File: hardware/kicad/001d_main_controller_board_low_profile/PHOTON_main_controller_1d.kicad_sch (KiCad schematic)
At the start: 61 parts, among them J1 JST_SH, J2 JST_SH, J3 USB_C_Receptacle_USB2.0, SW1 SW_SPST, SW2 SW_SPST, U1 RP2350_60QFN, U2 NCP1117-3.3_SOT223, U3 W25Q128JVPIQ, U4 TPD4E05U06DQAR, U5 THVD1424RGTR, Y1 ABM8-272-T3

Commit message: Main Controller Board (1D) now added. Cheaper design, with RP2354, and BUCK PMIC
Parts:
- removed C22: 100nF, Capacitor_SMD:C_0402_1005Metric, symbol Device:C
- removed H1, H2, H3, H4: MountingHole, MountingHole:MountingHole_2.7mm_M2.5, symbol Mechanical:MountingHole
- removed J2: JST_SH, Connector_JST:JST_SH_SM04B-SRSS-TB_1x04-1MP_P1.00mm_Horizontal, symbol Connector_Generic:Conn_01x04
- removed J4: (no value), Connector_PinHeader_1.27mm:PinHeader_1x04_P1.27mm_Vertical, symbol Connector_Generic:Conn_01x04
- removed JP101: SolderJumper_2_Open, Jumper:SolderJumper-2_P1.3mm_Open_RoundedPad1.0x1.5mm, symbol Jumper:SolderJumper_2_Open
- removed JP2: SolderJumper_2_Bridged, Jumper:SolderJumper-2_P1.3mm_Bridged_RoundedPad1.0x1.5mm, symbol Jumper:SolderJumper_2_Bridged
- removed R13, R14: 22Ω, Resistor_SMD:R_0402_1005Metric, symbol Device:R
- removed R15: DNF, Resistor_SMD:R_0402_1005Metric, symbol Device:R
- removed R17: 100kΩ, Resistor_SMD:R_0402_1005Metric, symbol Device:R
- removed R4: 120 Ω, Resistor_SMD:R_0402_1005Metric, symbol Device:R
- removed SW1, SW2: SW_SPST, footprints:SW-TH_MSK12C02, symbol spst:MSK12C02
- removed U2: NCP1117-3.3_SOT223, Package_TO_SOT_SMD:SOT-223-3_TabPin2, symbol Regulator_Linear:NCP1117-3.3_SOT223
- removed U3: W25Q128JVPIQ, footprints:WSON_128JVPIQ_WIN, symbol Memory_Flash:W25Q128JVS
- removed U5: THVD1424RGTR, footprints:QFN_24RGTR_TEX, symbol 2025-11-21_08-29-10_THVD1424RGTR:THVD1424RGTR
- added C105: 100nF, Capacitor_SMD:C_0402_1005Metric, symbol Device:C
- added C106: 1μF, Capacitor_SMD:C_0402_1005Metric, symbol Device:C
- added CR101: H7VHD3UA, Diode_SMD:D_SOD-323, symbol 2025-08-11_08-49-29:SMF5.0A
- added D10, D11: D_TVS, Diode_SMD:D_SOD-523, symbol Device:D_Schottky
- added H101, H102, H103, H104: MountingHole, MountingHole:MountingHole_2.7mm_M2.5_ISO7380, symbol Mechanical:MountingHole
- added J102: JST_SH RS-485_1, Connector_JST:JST_SH_SM04B-SRSS-TB_1x04-1MP_P1.00mm_Horizontal, symbol Connector_Generic:Conn_01x04
- added J103, J104: JST_SH RS-485_2, Connector_JST:JST_SH_SM04B-SRSS-TB_1x04-1MP_P1.00mm_Horizontal, symbol Connector_Generic:Conn_01x04
- added J4: Micro_SD_Card, Pretty Custom:TF-015_corrected, symbol Connector:Micro_SD_Card
- added JP101: Jumper_2_Open, Jumper:SolderJumper-2_P1.3mm_Open_Pad1.0x1.5mm, symbol Jumper:Jumper_2_Open
- added L2: 1 uH, Inductor_SMD:L_1008_2520Metric, symbol Device:L
- added R103: 100kΩ, Resistor_SMD:R_0402_1005Metric, symbol Device:R
- added R104: 300kΩ, Resistor_SMD:R_0402_1005Metric, symbol Device:R
- added R105: 150kΩ, Resistor_SMD:R_0402_1005Metric, symbol Device:R
- added R236, R237: 2.2kΩ, Resistor_SMD:R_0402_1005Metric, symbol Device:R
- added U102: THVD1424RGTR, Pretty Custom:QFN_24RGTR_TEX, symbol 2025-11-21_08-29-10_THVD1424RGTR:THVD1424RGTR
- added U5: TPS62A0569ADRLR, Pretty Custom:DRL0006A-MFG, symbol TI BUCK:TPS62A0569ADRLR
- C1: value 10uF -> 4.7uF; JLCPCB Part # (none) -> C1779; Part # (none) -> CL21A475KAQNNNE
- C2, C3: footprint footprints:C_0402_1005Metric_small_pads -> RP2350_60QFN_minimal:C_0402_1005Metric_small_pads
- C4: value 10uF -> 22uF; JLCPCB Part # (none) -> C45783
- CR1: value PTVSHC3D7VU -> H7VHD3UA; footprint footprints:SOD-323_L1.8-W1.3-LS2.5-RD -> Diode_SMD:D_SOD-323; symbol PTVSHC3D7VU:PTVSHC3D7VU -> 2025-08-11_08-49-29:SMF5.0A; LCSC Part C110753 -> (none)
- CR5: renamed from CR2; value PTVSHC3D7VU -> H7VHD3UA; footprint footprints:SOD-323_L1.8-W1.3-LS2.5-RD -> Diode_SMD:D_SOD-323; symbol PTVSHC3D7VU:PTVSHC3D7VU -> 2025-08-11_08-49-29:SMF5.0A; LCSC Part C110753 -> (none)
- L1: footprint footprints:L_pol_2016 -> RP2350_60QFN_minimal:L_pol_2016
- R101: value 120 Ω -> 22Ω
- R102: value 10kΩ -> 33Ω
- U1: value RP2350_60QFN -> RP2354_60QFN; footprint footprints:RP2350-QFN-60-1EP_7x7_P0.4mm_EP3.4x3.4mm_ThermalVias -> RP2350_60QFN_minimal:RP2350-QFN-60-1EP_7x7_P0.4mm_EP3.4x3.4mm_ThermalVias; JLCPCB Part # C42411118 -> C41378174
- U4: footprint footprints:DQA0010A -> Pretty Custom:DQA0010A
- renumbered C9 to C103, C10 to C104, J1 to J101, R20 to R233
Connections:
- net +3V3: now also C105.1, C106.1, CR101.1, J102.2 (Pin_2), J103.2 (Pin_2), J104.2 (Pin_2), J4.4 (VDD), L2.2, R104.1, R236.2, R237.2, U102.13 (VIO), U102.14 (VCC), U102.15 (H/F); no longer R102.2
- net GND: now also C105.2, C106.2, CR101.2, D10.2 (A), D11.2 (A), J102.1 (Pin_1), J103.1 (Pin_1), J104.1 (Pin_1), J4.6 (VSS), JP101.1 (A), R103.2, U102.17 (GND), U102.6 (GND), U5.2 (GND)
- net GPIO10: now also J4.5 (CLK)
- net GPIO11: now also J4.3 (CMD)
- net GPIO12: now also J4.7 (DAT0)
- net GPIO13: now also J4.2 (DAT3/CD)
- net GPIO16: now also R101.2
- net GPIO17: now also R102.2
- net GPIO18: now also U102.5 (TERM_TX), U102.7 (TERM_RX)
- net GPIO22: no longer R19.2
- net GPIO23: no longer R233.2
- net GPIO4: now also R19.2
- net RS485_N: now also J102.4 (Pin_4), J103.4 (Pin_4), J104.4 (Pin_4), U102.10 (Z); no longer J101.4 (Pin_4)
- net RS485_P: now also J102.3 (Pin_3), J103.3 (Pin_3), J104.3 (Pin_3), U102.9 (Y); no longer J101.3 (Pin_3), R101.2
- net RUN: no longer R102.1
- net UART_RX: now also U102.1 (R)
- net UART_TX: now also U102.4 (D)
- net ~{USB_BOOT}: now also JP101.2 (B)
- net at C1.1, FB1.2: now also U5.3 (VIN), U5.5 (EN)
- net I2C_0_SDA: now reaches R101.1
- net I2C_0_SDA: now also J101.3 (Pin_3), D10.1 (K), R236.1
- net BANK_0_CS renamed GPIO21
- net BANK_1_CS renamed GPIO20
- net BANK_2_CS renamed GPIO19
- net BANK_3_CS renamed GPIO15
- net BANK_4_CS renamed GPIO1
- net GPIO1: now also U102.2 (RE), U102.3 (DE)
- net BANK_5_CS renamed GPIO7
- net BANK_6_CS renamed GPIO5
- net GPIO5: now also R233.2
- net BANK_7_CS renamed GPIO6
- net FLASH_SS renamed QSPI_SS
- new net: R103.1, R105.2, U5.1 (FB)
- new net: L2.1, U5.4 (SW)
- new net: R104.2, R105.1
- new net I2C_0_SCL: D11.1 (K), J101.4 (Pin_4), R102.1, R237.1
- no-connect marks 7 -> 8
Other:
- removed sheet Sensor Array
- note added: "I2C (Qwiic) Interfaces"
- note added: "Inter-board RS-485 UART Interface"
- note added: "Power"
- note added: "RS485 needs a termination at the end of the bus. A middle device with both left and right connected needs to have both ends unterminated. But if it's at the end of the bus, and JST right is used, then drive RS485_TERM high. If end-fed by JST left, then right must be terminated"
- note removed: "Cut for backpower issues when USB power is not used. Note: When cut, board is no longer able to be powered by USB."
- note removed: "Debug Connector"
- note removed: "Flash"
- note removed: "Left"
- note removed: "Power and USB"
- note removed: "RS-485 Interface"
- note removed: "Right"
- note removed: "Sensor Array"
- note removed: "Short to force USB Bootloader"
- note removed: "Terminate (right position) when connector is not used."
- note removed: "This built-in RS485 termination should not be used. Rather, terminate at the end of the board using the switches."
- title: PHOTON Sensor Board - 002 -> PHOTON Main Controller Board A004
- moved on the sheet: C1, C103, C104, C13, C14, C15, C16, C17, C18, C19, C2, C20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

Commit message: 001d 3.3V version committed.
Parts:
- U4: footprint Pretty Custom:DQA0010A -> footprints:DQA0010A
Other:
- moved on the sheet: C4, D3, L2, R104, R105, R8, U5

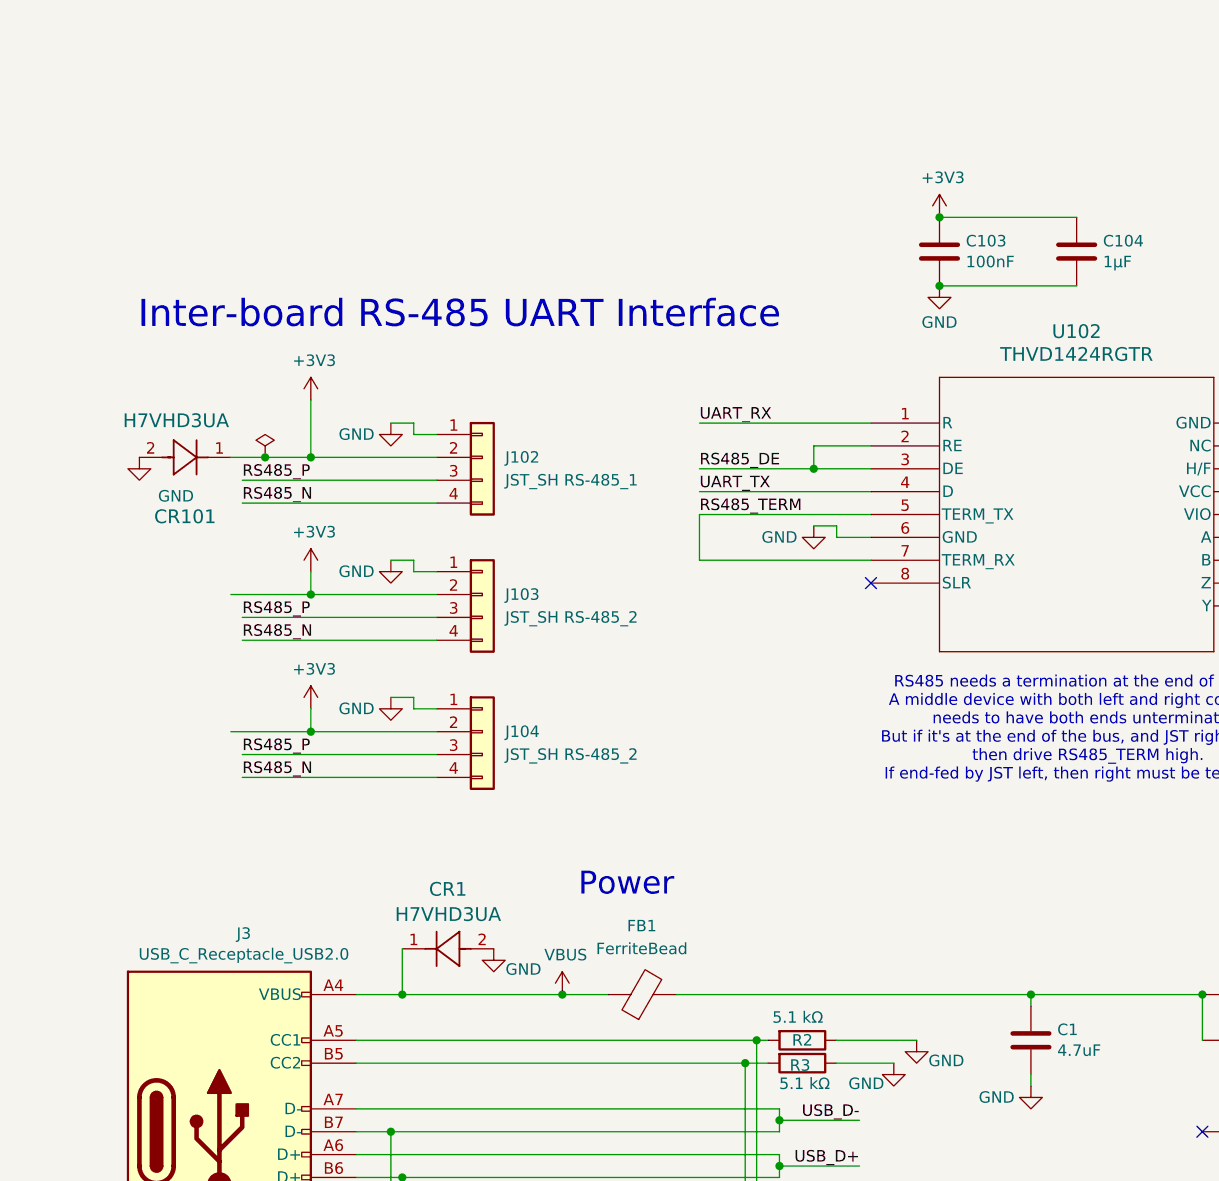
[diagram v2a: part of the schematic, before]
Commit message: 001d bumped to 5V RS485 bus voltage. Sensor board schematic cleaned up, layout not begun
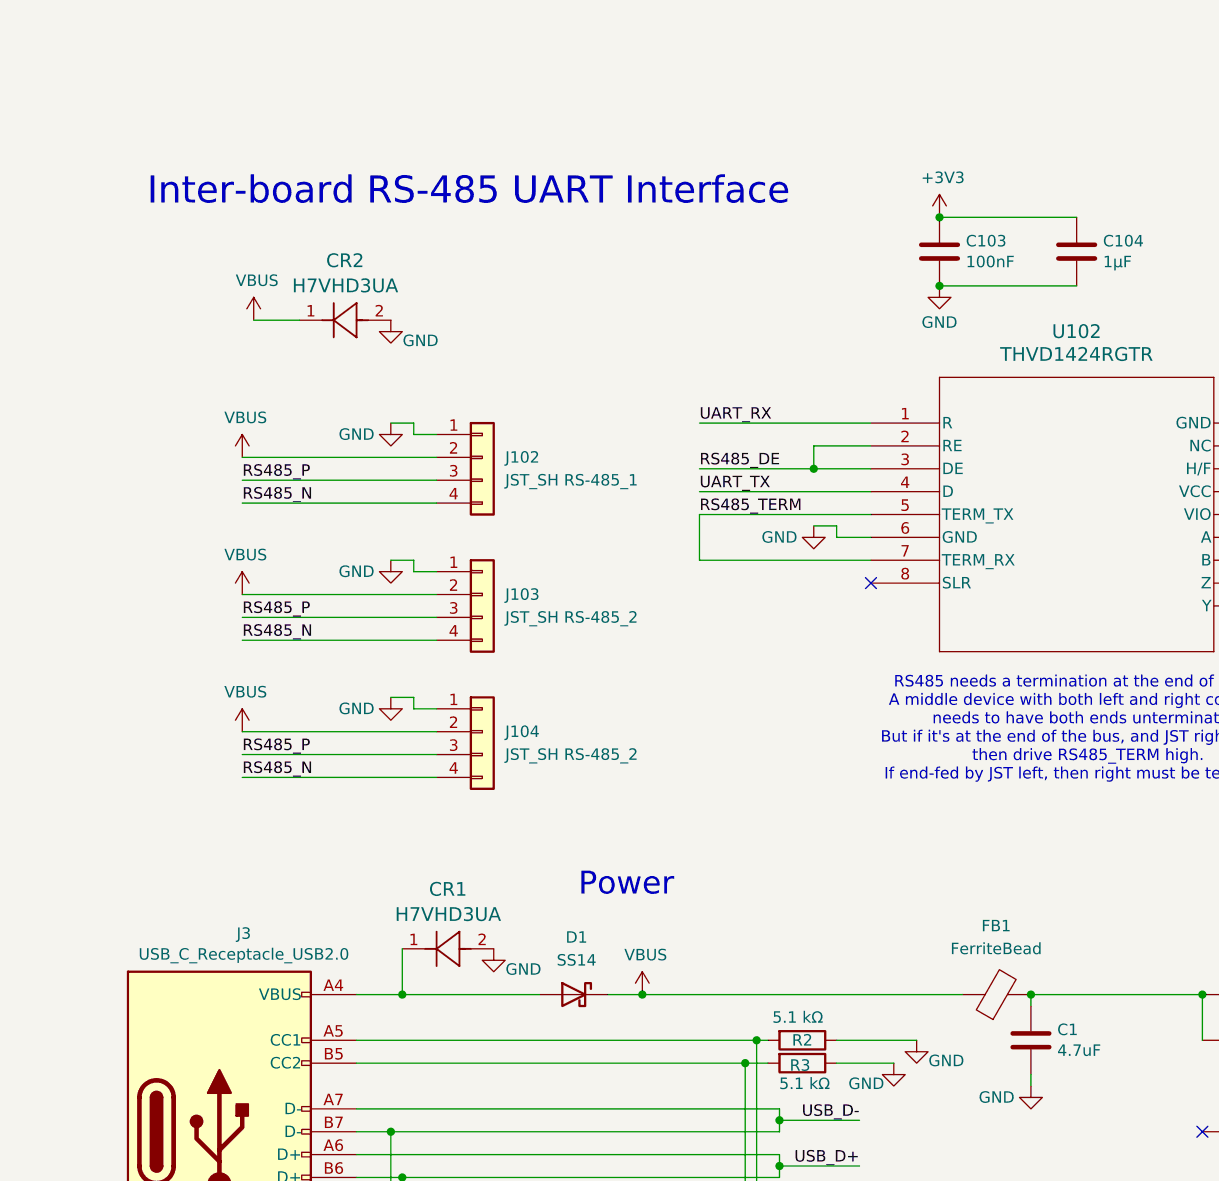
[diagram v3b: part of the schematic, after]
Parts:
- removed CR101: H7VHD3UA, Diode_SMD:D_SOD-323, symbol 2025-08-11_08-49-29:SMF5.0A
- added CR2: H7VHD3UA, Diode_SMD:D_SOD-323, symbol 2025-08-11_08-49-29:SMF5.0A
- added D1: SS14, Diode_SMD:D_SMA, symbol Device:D_Schottky
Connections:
- net +3V3: no longer J102.2 (Pin_2), J103.2 (Pin_2), J104.2 (Pin_2)
- net GND: now also CR2.2
- net VBUS: now also J102.2 (Pin_2), J103.2 (Pin_2), J104.2 (Pin_2), CR2.1, D1.1 (K), D1.2 (A)
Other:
- moved on the sheet: FB1
